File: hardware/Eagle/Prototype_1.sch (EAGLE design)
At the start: 11 parts, among them IC1 MEGA32-P, Q1 16MHz

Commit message: Readme and Eagle Circuit Files updated
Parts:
- removed IC1: MEGA32-P, atmel:MEGA32-P
- removed ICSP: AVR_SPI_PRG_6PTH, SparkFun-Connectors:AVR_SPI_PRG_6PTH
- added INPUT: USB-A, adafruit:USB-A
- added ISP1: AVRISP-6, adafruit:AVRISP-6
- added MCU: ATmega328P, adafruit:ATMEGA168-20P
- added OUTPUT: USB-MICRO-B, SparkFun-Connectors:USB_MICROB_PLUGCONN-11752
- added POTI, POTI1: MCP41XXXDIL, SparkFun-AnalogIC:MCP41XXXDIL
- FTDI: value FTDI_BASICPTH -> (none); device SparkFun-Connectors:FTDI_BASICPTH -> SparkFun-Connectors:ARDUINO_SERIAL_PROGRAMPTH
- RESET: value RACON12 -> (none); device switch-misc:RACON12 -> switch-omron:31-XX
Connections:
- removed net N$12: IC1.(MOSI)PB5, ICSP.4
- removed net N$6: FTDI.3, IC1.(RXD)PD0
- removed net N$7: R2.1, RESET.S
- removed net N$9: IC1.(MISO)PB6, ICSP.1
- new net MISO: ISP1.MISO, MCU.(PCI4/MISO)PB4
- new net MOSI: ISP1.MOSI, MCU.(PCI3/MOSI/OC2A)PB3, POTI.DI, POTI1.DI
- new net N$10: MCU.(PCI10/ADC2)PC2, OUTPUT.D+, POTI1.W
- new net N$11: MCU.(PCI11/ADC3)PC3, OUTPUT.D-, POTI.W
- new net N$14: INPUT.D+, MCU.(PCI8/ADC0)PC0
- new net N$15: INPUT.D-, MCU.(PCI9/ADC1)PC1
- new net SCK: ISP1.SCK, MCU.(PCI5/SCK)PB5, POTI.SCK, POTI1.SCK
- net +5V: now also C3.1, C4.1, FTDI.VCC, INPUT.VBUS, ISP1.VCC, MCU.AVCC, MCU.VCC, OUTPUT.VCC, POTI.B, POTI.VCC, POTI1.B, POTI1.VCC, R2.1; no longer C3.2, C4.2, FTDI.4, IC1.AVCC, IC1.VCC, ICSP.2, R2.2
- net GND: now also C3.2, C4.2, FTDI.CTS, FTDI.GND, INPUT.GND, ISP1.GND, MCU.AGND, MCU.GND, OUTPUT.GND, OUTPUT.SHIELD, POTI.A, POTI.GND, POTI1.A, POTI1.GND; no longer C3.1, C4.1, FTDI.5, FTDI.6, IC1.GND, IC1.GND@1, ICSP.6, RESET.P@1
- net N$1: now also C1.2, MCU.PB6(XTAL1/TOSC1/PCI6), Q1.2; no longer C2.2, IC1.XTAL1, Q1.1
- net N$2: now also C2.2, MCU.PB7(XTAL2/TOSC2/PCI7), Q1.1; no longer C1.2, IC1.XTAL2, Q1.2
- net N$3: now also FTDI.TXO, MCU.(PCI16/RXD)PD0; no longer C5.2, FTDI.1
- net N$4: now also ISP1.RST, MCU.PC6(/RESET/PCI14), R2.2, RESET.S; no longer IC1.RESET, ICSP.5, RESET.S@1
- net N$5: now also FTDI.RXI, MCU.(PCI17/TXD)PD1; no longer FTDI.2, IC1.(TXD)PD1
- net N$8: now also C5.2, FTDI.DTR; no longer IC1.(SCK)PB7, ICSP.3
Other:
- moved on the sheet: C1, C2, C3, C4, C5, FTDI, Q1, R2

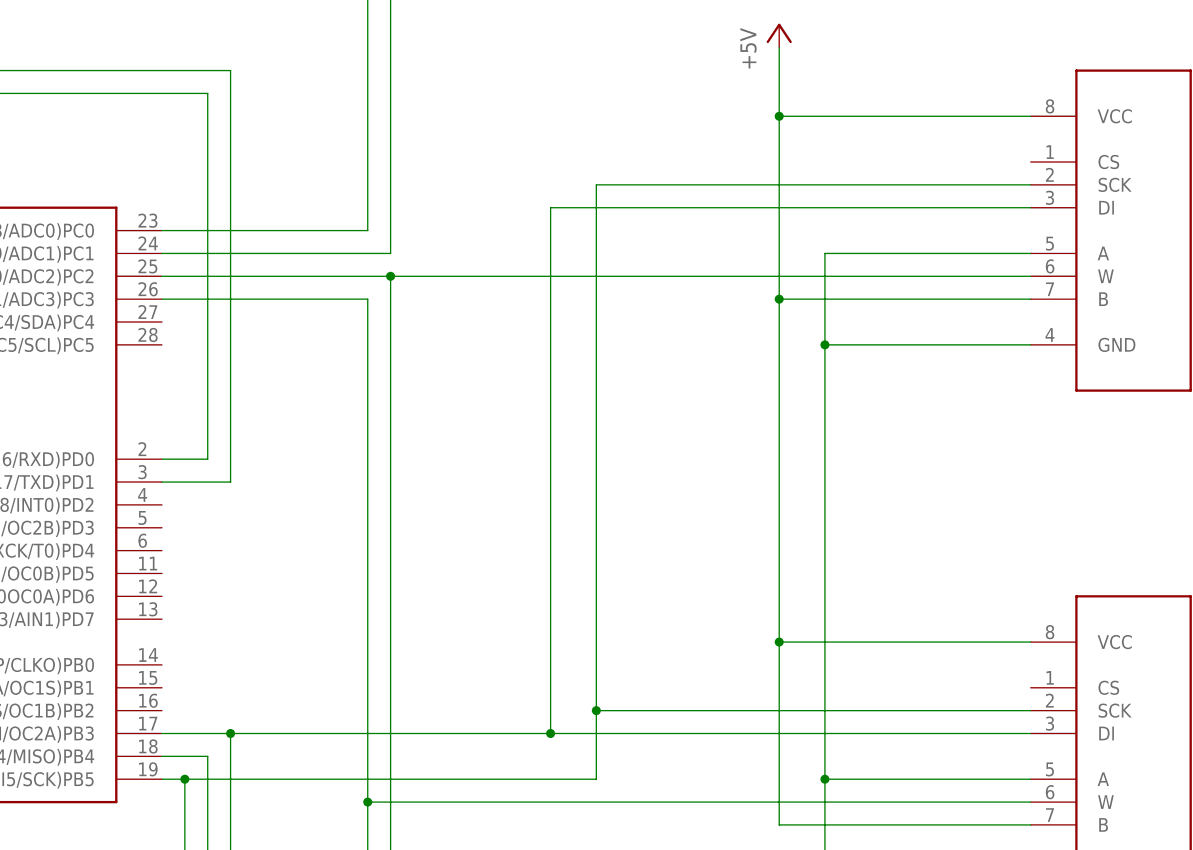
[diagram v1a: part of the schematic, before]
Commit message: CS connected
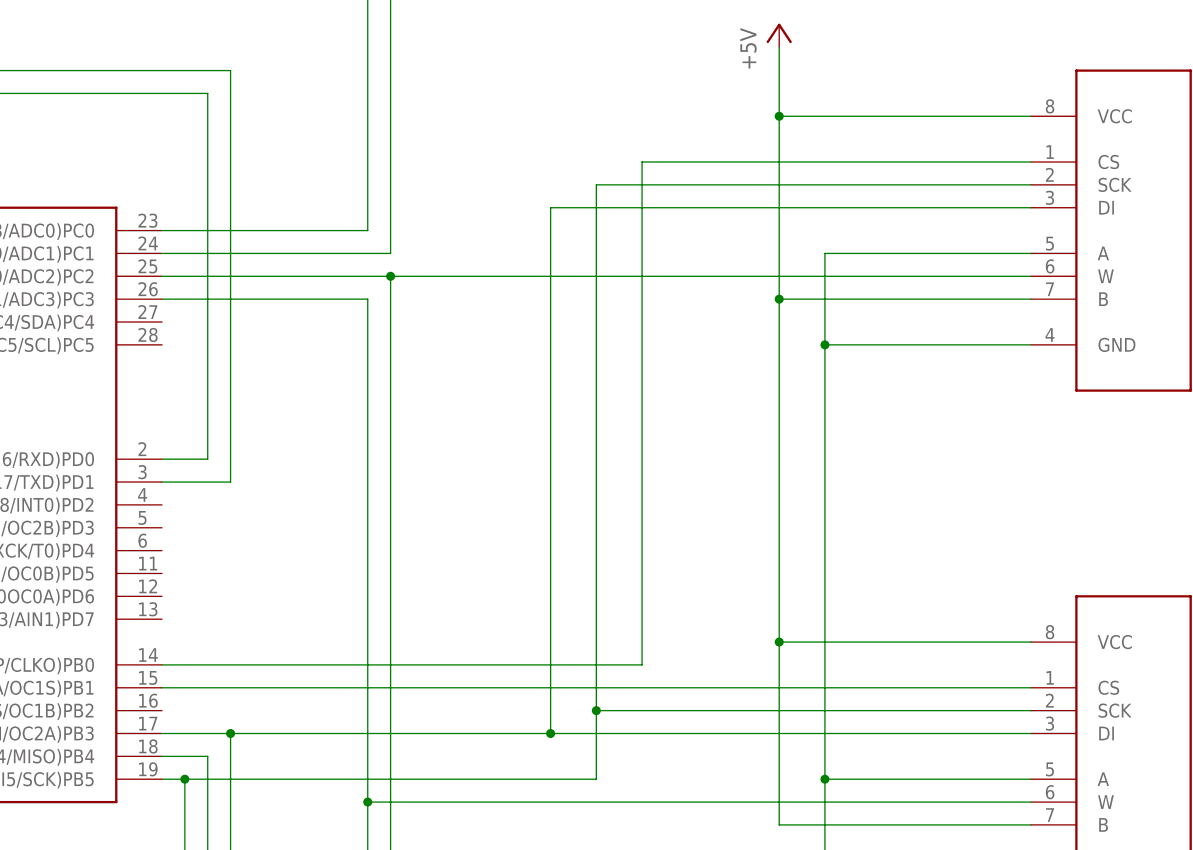
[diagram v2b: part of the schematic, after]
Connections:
- new net N$6: MCU.(PCI0/ICP/CLKO)PB0, POTI1.CS
- new net N$7: MCU.(PCI1/OC1A/OC1S)PB1, POTI.CS
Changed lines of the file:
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@@
+</segment>
+</net>
+<net name="N$6" class="0">
+<segment>
+<pinref part="MCU" gate="G$1" pin="(PCI0/ICP/CLKO)PB0"/>
+<wire x1="33.02" y1="-20.32" x2="86.36" y2="-20.32" width="0.1524" layer="91"/>
+<wire x1="86.36" y1="-20.32" x2="86.36" y2="35.56" width="0.1524" layer="91"/>
+<pinref part="POTI1" gate="G$1" pin="CS"/>
+<wire x1="86.36" y1="35.56" x2="129.54" y2="35.56" width="0.1524" layer="91"/>
+</segment>
+</net>
+<net name="N$7" class="0">
+<segment>
+<pinref part="MCU" gate="G$1" pin="(PCI1/OC1A/OC1S)PB1"/>
+<pinref part="POTI" gate="G$1" pin="CS"/>
+<wire x1="33.02" y1="-22.86" x2="129.54" y2="-22.86" width="0.1524" layer="91"/>
 </segment>
 </net>

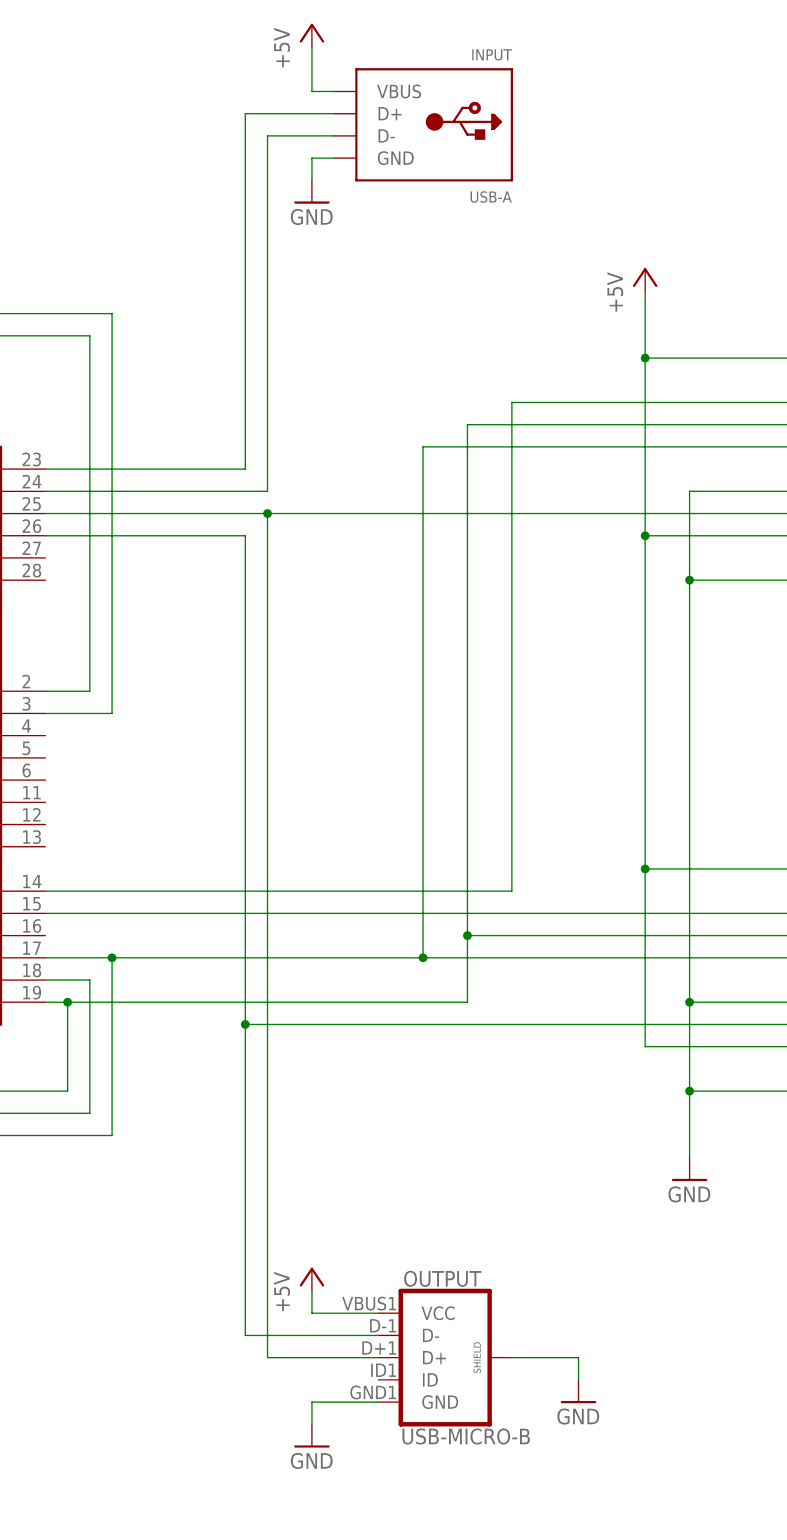
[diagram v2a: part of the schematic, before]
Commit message: Correct USB connectors in circuit
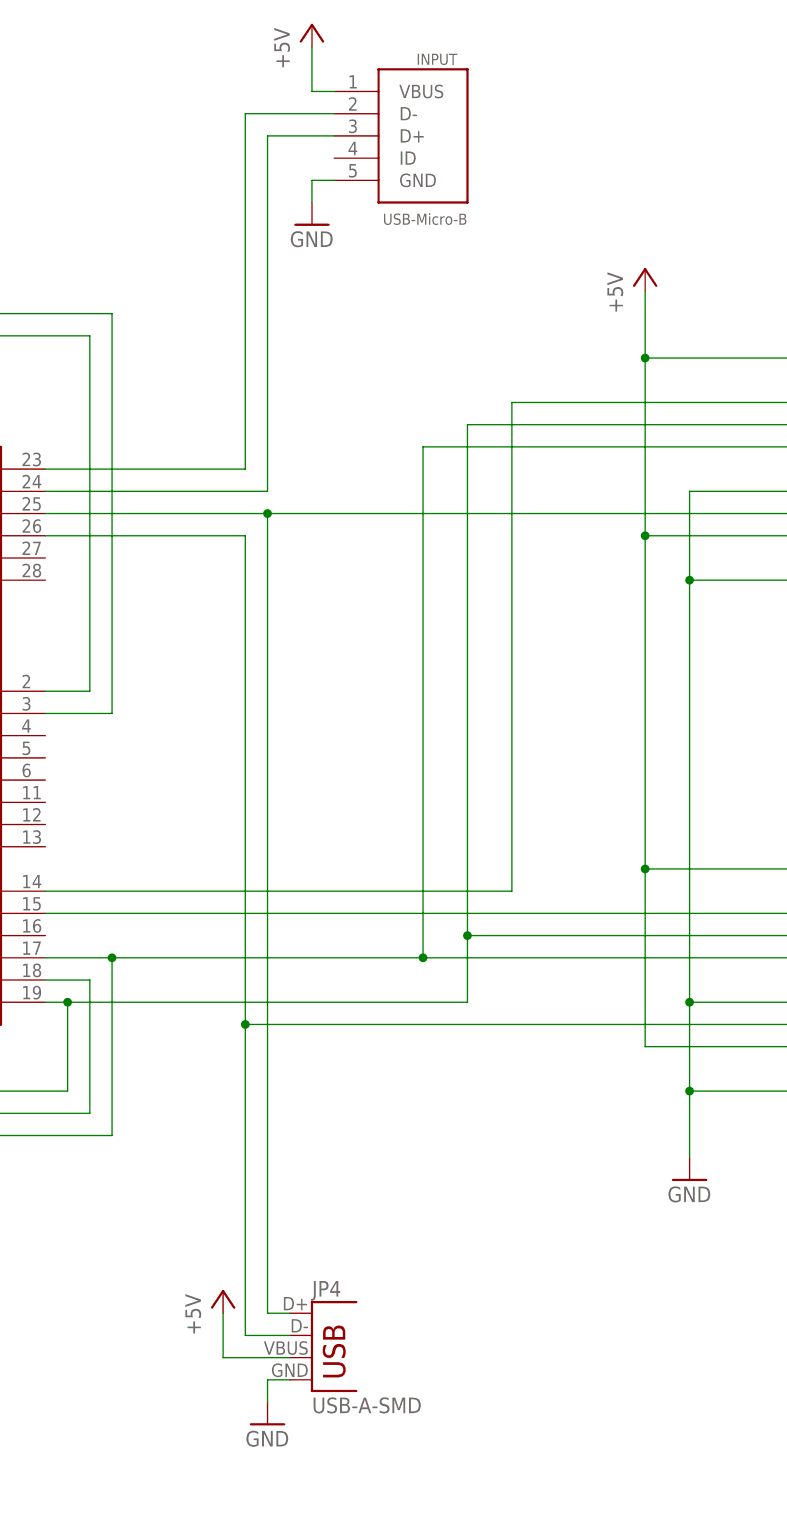
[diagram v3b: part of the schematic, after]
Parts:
- removed OUTPUT: USB-MICRO-B, SparkFun-Connectors:USB_MICROB_PLUGCONN-11752
- added JP4: USB-A-SMD, SparkFun-Connectors:USB-A-SMD
- INPUT: value USB-A -> USB-Micro-B; device adafruit:USB-A -> GeekAmmo:USB-CON-5PIN-105017-0001
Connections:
- net +5V: now also JP4.VBUS; no longer OUTPUT.VCC
- net GND: now also JP4.GND; no longer OUTPUT.GND, OUTPUT.SHIELD
- net N$10: now also JP4.D+; no longer OUTPUT.D+
- net N$11: now also JP4.D-; no longer OUTPUT.D-
- net N$14: now also INPUT.D-; no longer INPUT.D+
- net N$15: now also INPUT.D+; no longer INPUT.D-
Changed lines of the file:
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@@
 <part name="GND7" library="supply1" deviceset="GND" device=""/>
 <part name="P+6" library="supply1" deviceset="+5V" device=""/>
-<part name="INPUT" library="adafruit" deviceset="USB-A" device=""/>
 <part name="GND8" library="supply1" deviceset="GND" device=""/>
 <part name="P+7" library="supply1" deviceset="+5V" device=""/>
 <part name="P+8" library="supply1" deviceset="+5V" device=""/>
 <part name="GND9" library="supply1" deviceset="GND" device=""/>
-<part name="OUTPUT" library="SparkFun-Connectors" deviceset="USB_MICROB_PLUG" device="CONN-11752" value="USB-MICRO-B"/>
-<part name="GND10" library="supply1" deviceset="GND" device=""/>
+<part name="JP4" library="SparkFun-Connectors" deviceset="USB" device="-A-SMD"/>
+<part name="INPUT" library="GeekAmmo" deviceset="USB-CON-5PIN" device="-105017-0001" value="USB-Micro-B"/>
 </parts>
 <sheets>
@@
 <instance part="GND7" gate="1" x="106.68" y="-53.34"/>
 <instance part="P+6" gate="1" x="101.6" y="50.8"/>
+<instance part="GND8" gate="1" x="58.42" y="-81.28"/>
+<instance part="P+7" gate="1" x="53.34" y="-66.04"/>
+<instance part="P+8" gate="1" x="63.5" y="78.74"/>
+<instance part="GND9" gate="1" x="63.5" y="55.88"/>
+<instance part="JP4" gate="G$1" x="63.5" y="-76.2"/>
 <instance part="INPUT" gate="G$1" x="76.2" y="66.04" rot="MR0"/>
-<instance part="GND8" gate="1" x="63.5" y="-83.82"/>
-<instance part="P+7" gate="1" x="63.5" y="-63.5"/>
-<instance part="P+8" gate="1" x="63.5" y="78.74"/>
-<instance part="GND9" gate="1" x="63.5" y="58.42"/>
-<instance part="OUTPUT" gate="G$1" x="78.74" y="-73.66"/>
-<instance part="GND10" gate="1" x="93.98" y="-78.74"/>
 </instances>
 <busses>
@@
 </segment>
 <segment>
+<pinref part="GND9" gate="1" pin="GND"/>
+<wire x1="63.5" y1="58.42" x2="63.5" y2="60.96" width="0.1524" layer="91"/>
+<wire x1="63.5" y1="60.96" x2="66.04" y2="60.96" width="0.1524" layer="91"/>
+<pinref part="INPUT" gate="G$1" pin="GND"/>
+</segment>
+<segment>
+<pinref part="JP4" gate="G$1" pin="GND"/>
 <pinref part="GND8" gate="1" pin="GND"/>
-<wire x1="63.5" y1="-81.28" x2="63.5" y2="-78.74" width="0.1524" layer="91"/>
-<pinref part="OUTPUT" gate="G$1" pin="GND"/>
-<wire x1="63.5" y1="-78.74" x2="71.12" y2="-78.74" width="0.1524" layer="91"/>
-</segment>
-<segment>
-<pinref part="GND9" gate="1" pin="GND"/>
-<wire x1="63.5" y1="60.96" x2="63.5" y2="63.5" width="0.1524" layer="91"/>
-<pinref part="INPUT" gate="G$1" pin="GND"/>
-<wire x1="63.5" y1="63.5" x2="66.04" y2="63.5" width="0.1524" layer="91"/>
-</segment>
-<segment>
-<pinref part="OUTPUT" gate="G$1" pin="SHIELD"/>
-<wire x1="86.36" y1="-73.66" x2="93.98" y2="-73.66" width="0.1524" layer="91"/>
-<pinref part="GND10" gate="1" pin="GND"/>
-<wire x1="93.98" y1="-73.66" x2="93.98" y2="-76.2" width="0.1524" layer="91"/>
+<wire x1="60.96" y1="-76.2" x2="58.42" y2="-76.2" width="0.1524" layer="91"/>
+<wire x1="58.42" y1="-76.2" x2="58.42" y2="-78.74" width="0.1524" layer="91"/>
 </segment>
 </net>
@@
 </segment>
 <segment>
-<pinref part="P+7" gate="1" pin="+5V"/>
-<wire x1="63.5" y1="-66.04" x2="63.5" y2="-68.58" width="0.1524" layer="91"/>
-<pinref part="OUTPUT" gate="G$1" pin="VCC"/>
-<wire x1="63.5" y1="-68.58" x2="71.12" y2="-68.58" width="0.1524" layer="91"/>
-</segment>
-<segment>
 <pinref part="P+8" gate="1" pin="+5V"/>
 <wire x1="63.5" y1="76.2" x2="63.5" y2="71.12" width="0.1524" layer="91"/>
+<wire x1="63.5" y1="71.12" x2="66.04" y2="71.12" width="0.1524" layer="91"/>
 <pinref part="INPUT" gate="G$1" pin="VBUS"/>
-<wire x1="63.5" y1="71.12" x2="66.04" y2="71.12" width="0.1524" layer="91"/>
+</segment>
+<segment>
+<pinref part="JP4" gate="G$1" pin="VBUS"/>
+<pinref part="P+7" gate="1" pin="+5V"/>
+<wire x1="60.96" y1="-73.66" x2="53.34" y2="-73.66" width="0.1524" layer="91"/>
+<wire x1="53.34" y1="-73.66" x2="53.34" y2="-68.58" width="0.1524" layer="91"/>
 </segment>
 </net>
@@
 <pinref part="MCU" gate="G$1" pin="(PCI10/ADC2)PC2"/>
 <wire x1="33.02" y1="22.86" x2="58.42" y2="22.86" width="0.1524" layer="91"/>
-<wire x1="58.42" y1="22.86" x2="58.42" y2="-73.66" width="0.1524" layer="91"/>
+<wire x1="58.42" y1="22.86" x2="58.42" y2="-68.58" width="0.1524" layer="91"/>
 <junction x="58.42" y="22.86"/>
-<pinref part="OUTPUT" gate="G$1" pin="D+"/>
-<wire x1="71.12" y1="-73.66" x2="58.42" y2="-73.66" width="0.1524" layer="91"/>
+<wire x1="60.96" y1="-68.58" x2="58.42" y2="-68.58" width="0.1524" layer="91"/>
+<pinref part="JP4" gate="G$1" pin="D+"/>
 </segment>
 </net>
@@
 <wire x1="55.88" y1="20.32" x2="33.02" y2="20.32" width="0.1524" layer="91"/>
 <junction x="55.88" y="-35.56"/>
-<pinref part="OUTPUT" gate="G$1" pin="D-"/>
-<wire x1="71.12" y1="-71.12" x2="55.88" y2="-71.12" width="0.1524" layer="91"/>
+<wire x1="60.96" y1="-71.12" x2="55.88" y2="-71.12" width="0.1524" layer="91"/>
+<pinref part="JP4" gate="G$1" pin="D-"/>
 </segment>
 </net>
@@
 <wire x1="33.02" y1="27.94" x2="55.88" y2="27.94" width="0.1524" layer="91"/>
 <wire x1="55.88" y1="27.94" x2="55.88" y2="68.58" width="0.1524" layer="91"/>
-<pinref part="INPUT" gate="G$1" pin="D+"/>
 <wire x1="55.88" y1="68.58" x2="66.04" y2="68.58" width="0.1524" layer="91"/>
+<pinref part="INPUT" gate="G$1" pin="D-"/>
 </segment>
 </net>
@@
 <wire x1="33.02" y1="25.4" x2="58.42" y2="25.4" width="0.1524" layer="91"/>
 <wire x1="58.42" y1="25.4" x2="58.42" y2="66.04" width="0.1524" layer="91"/>
-<pinref part="INPUT" gate="G$1" pin="D-"/>
 <wire x1="58.42" y1="66.04" x2="66.04" y2="66.04" width="0.1524" layer="91"/>
-</segment>
-</net>
+<pinref part="INPUT" gate="G$1" pin="D+"/>
+</segment>
+</net>
